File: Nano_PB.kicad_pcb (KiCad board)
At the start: 2 copper layers, 100 x 50 mm, 134 parts, among them CON1 BARREL_JACK, P1 CONN_02X04, P10 CONN_01X04, P11 CONN_01X04, P12 CONN_01X04, P2 CONN_01X06, P3 CONN_01X01, P4 CONN_01X03, P5 CONN_01X03, P6 CONN_01X03, P7 CONN_01X03, P8 CONN_01X03, P9 CONN_01X04, Q1 SMBT3904, Q2 SMBT3904, Q3 SMBT3904, Q4 SMBT3904, Q5 SMBT3904, Q6 BSS138, Q7 BSS138, SW1 Izquierda, SW2 Arriba, SW3 Abajo, SW4 Derecha, U1 Arduino_Nano, U2 LM7805CT, U3 74HC595, U4 74HC595, U5 Matriz_5x7, U6 PCA9551, U7 74HC148, U8 MMA7660FC, U9 40106

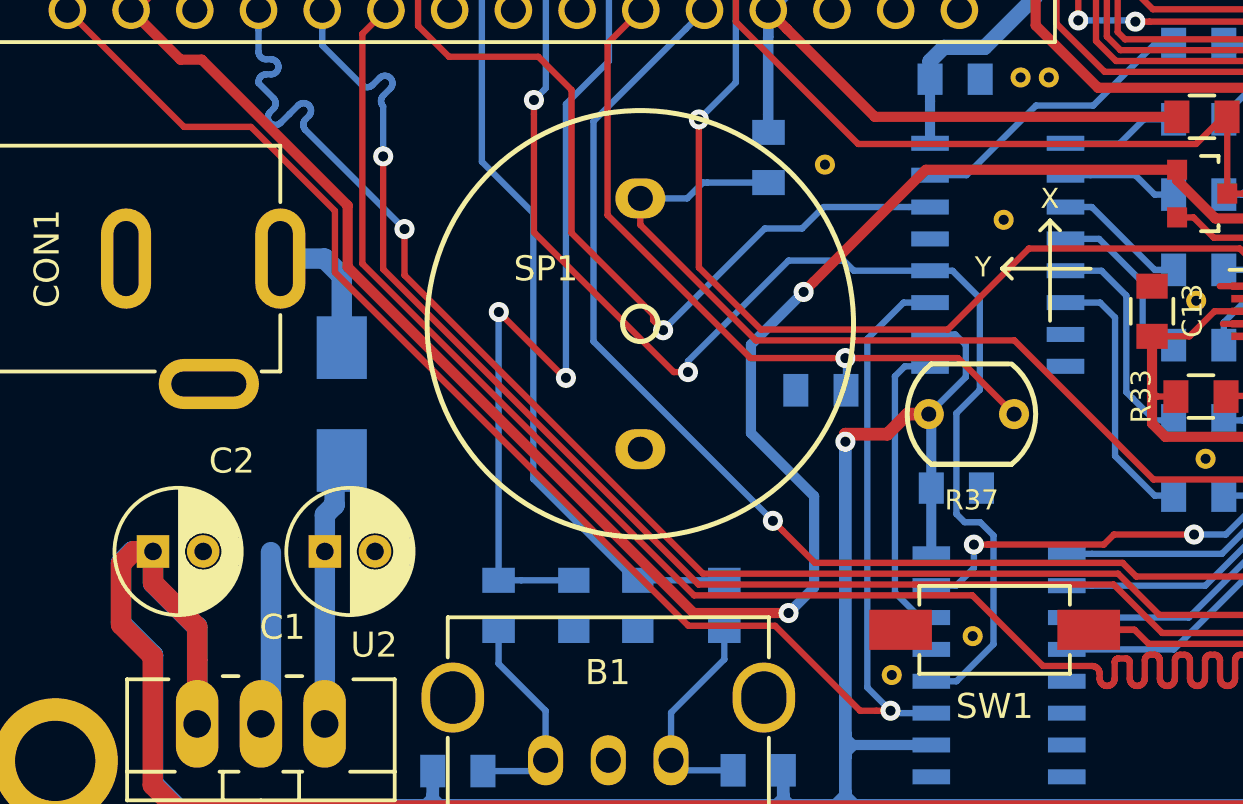
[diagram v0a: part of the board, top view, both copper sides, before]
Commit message: completar serigrafias
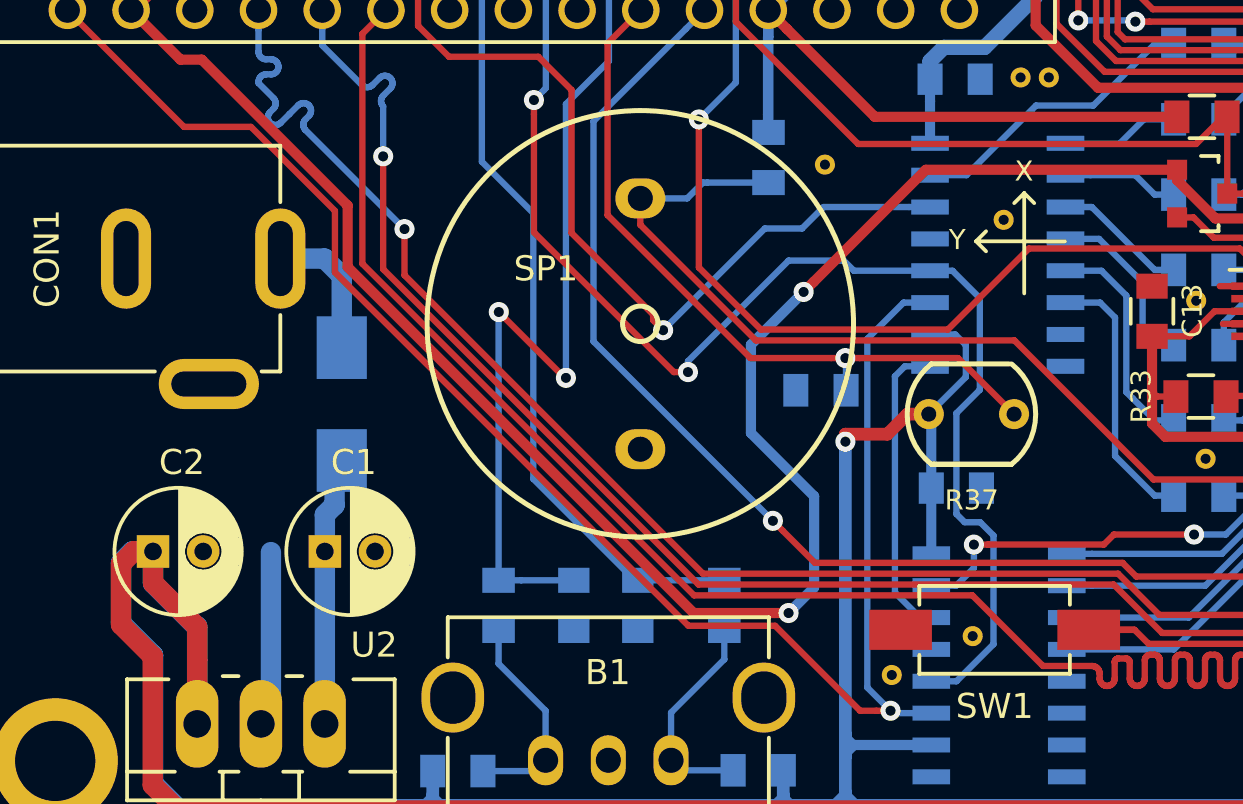
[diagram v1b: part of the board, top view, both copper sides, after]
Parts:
- moved G*** 1.10 mm to (62.9, 35.6)
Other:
- board text added: "3V3"
- board text added: "B0-A0"
- board text added: "B1-A1"
- board text added: "Bu-Ch5"
- board text added: "Buzz-Ch7"
- board text added: "Ch0"
- board text added: "Ch1"
- board text added: "Ch2"
- board text added: "Ch3"
- board text added: "ChB-D5"
- board text added: "Gn-Ch6"
- board text added: "Pul-A2"
- board text added: "Rd-Ch4"
- board text added: "TxD-D10 / RxD-D11"
- board text removed: "Bu-D11"
- board text removed: "Buzz-Ch8"
- board text removed: "Ch 1"
- board text removed: "Ch 2"
- board text removed: "Ch 3"
- board text removed: "Ch 4"
- board text removed: "ChB-A2"
- board text removed: "Gn-D10"
- board text removed: "Rd-D9"
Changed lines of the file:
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@@
     (links 268)
     (no_connects 0)
-    (area 49.508999 21.7677 161.770237 78.4273)
+    (area 52.014999 24.694999 152.165001 74.845001)
     (thickness 1.6)
-    (drawings 64)
+    (drawings 72)
     (tracks 1715)
     (zones 0)
@@
   )
   (module logos:KiCad-Logo_11mmx5mm (layer B.Cu)
-    (at 62.1 34.85 180)
+    (at 62.93 35.57 180)
     (fp_text reference G*** (at -0.8 1.6 180) (layer Cmts.User)
       (effects (font (size 0.3 0.3) (thickness 0.03)))
@@
     (descr "Radial Electrolytic Capacitor 5mm x Length 11mm, Pitch 2mm")
     (tags "Electrolytic Capacitor")
-    (fp_text reference C1 (at -1.69 3.02) (layer F.SilkS)
+    (fp_text reference C1 (at 1.15 -3.55) (layer F.SilkS)
       (effects (font (size 1 1) (thickness 0.15)))
     )
@@
     (descr "Radial Electrolytic Capacitor 5mm x Length 11mm, Pitch 2mm")
     (tags "Electrolytic Capacitor")
-    (fp_text reference C2 (at 3.14 -3.605) (layer F.SilkS)
+    (fp_text reference C2 (at 1.15 -3.55) (layer F.SilkS)
       (effects (font (size 1 1) (thickness 0.15)))
     )
@@
     )
   )
+  (gr_text Pul-A2 (at 130.856191 73.31) (layer B.SilkS)
+    (effects (font (size 1 1) (thickness 0.15)) (justify mirror))
+  )
+  (gr_text B1-A1 (at 131.094286 71.755) (layer B.SilkS)
+    (effects (font (size 1 1) (thickness 0.15)) (justify mirror))
+  )
+  (gr_text B0-A0 (at 131.094286 70.2) (layer B.SilkS)
+    (effects (font (size 1 1) (thickness 0.15)) (justify mirror))
+  )
+  (gr_text "TxD-D10 / RxD-D11" (at 104.85 26.58) (layer B.SilkS)
+    (effects (font (size 1 1) (thickness 0.15)) (justify mirror))
+  )
+  (gr_text Gnd (at 111.73 32.12) (layer B.SilkS)
+    (effects (font (size 1 1) (thickness 0.15)) (justify mirror))
+  )
+  (gr_text RxD (at 98.14 32) (layer B.SilkS)
+    (effects (font (size 1 1) (thickness 0.15)) (justify mirror))
+  )
+  (gr_text TxD (at 111.67 29.59) (layer B.SilkS)
+    (effects (font (size 1 1) (thickness 0.15)) (justify mirror))
+  )
+  (gr_text 3V3 (at 98.163809 29.43) (layer B.SilkS)
+    (effects (font (size 1 1) (thickness 0.15)) (justify mirror))
+  )
   (gr_text Izq-D6 (at 148.275 30.575) (layer B.SilkS)
     (effects (font (size 1 1) (thickness 0.15)) (justify mirror))
@@
     (effects (font (size 1 1) (thickness 0.15)) (justify mirror))
   )
-  (gr_text "Ch 1" (at 120.45 27.65) (layer B.SilkS)
+  (gr_text Ch0 (at 120.54 27.7) (layer B.SilkS)
     (effects (font (size 1 1) (thickness 0.15)) (justify mirror))
   )
-  (gr_text "Ch 2" (at 120.45 30.825) (layer B.SilkS)
+  (gr_text Ch1 (at 120.54 30.875) (layer B.SilkS)
     (effects (font (size 1 1) (thickness 0.15)) (justify mirror))
   )
@@
   (gr_line (start 52.09 24.77) (end 152.09 24.77) (layer Edge.Cuts) (width 0.15))
   (gr_line (start 52.09 34.77) (end 52.09 24.77) (layer Edge.Cuts) (width 0.15))
-  (gr_text Y (at 91.655 52.51) (layer F.SilkS)
+  (gr_text Y (at 90.625 51.42) (layer F.SilkS)
     (effects (font (size 0.8 0.8) (thickness 0.15)))
   )
-  (gr_text X (at 94.315 49.78) (layer F.SilkS)
+  (gr_text X (at 93.285 48.69) (layer F.SilkS)
     (effects (font (size 0.8 0.8) (thickness 0.15)))
   )
-  (gr_line (start 94.325 52.575) (end 95.945 52.575) (layer F.SilkS) (width 0.15))
-  (gr_line (start 92.405 52.57) (end 92.805 52.97) (layer F.SilkS) (width 0.15))
-  (gr_line (start 92.405 52.57) (end 92.805 52.17) (layer F.SilkS) (width 0.15))
-  (gr_line (start 94.325 52.57) (end 92.405 52.57) (layer F.SilkS) (width 0.15))
-  (gr_line (start 94.325 50.65) (end 94.725 51.05) (layer F.SilkS) (width 0.15))
-  (gr_line (start 93.925 51.05) (end 94.325 50.65) (layer F.SilkS) (width 0.15))
-  (gr_line (start 94.325 50.65) (end 94.325 54.65) (layer F.SilkS) (width 0.15))
-  (gr_text "Ch 3" (at 120.45 34) (layer B.SilkS)
+  (gr_line (start 93.295 51.485) (end 94.915 51.485) (layer F.SilkS) (width 0.15))
+  (gr_line (start 91.375 51.48) (end 91.775 51.88) (layer F.SilkS) (width 0.15))
+  (gr_line (start 91.375 51.48) (end 91.775 51.08) (layer F.SilkS) (width 0.15))
+  (gr_line (start 93.295 51.48) (end 91.375 51.48) (layer F.SilkS) (width 0.15))
+  (gr_line (start 93.295 49.56) (end 93.695 49.96) (layer F.SilkS) (width 0.15))
+  (gr_line (start 92.895 49.96) (end 93.295 49.56) (layer F.SilkS) (width 0.15))
+  (gr_line (start 93.295 49.56) (end 93.295 53.56) (layer F.SilkS) (width 0.15))
+  (gr_text Ch2 (at 120.54 34.05) (layer B.SilkS)
     (effects (font (size 1 1) (thickness 0.15)) (justify mirror))
   )
-  (gr_text "Ch 4" (at 120.45 37.175) (layer B.SilkS)
+  (gr_text Ch3 (at 120.54 37.225) (layer B.SilkS)
     (effects (font (size 1 1) (thickness 0.15)) (justify mirror))
   )
@@
     (effects (font (size 1 1) (thickness 0.15)) (justify mirror))
   )
-  (gr_text ChB-A2 (at 56.6 67.65) (layer B.SilkS)
+  (gr_text ChB-D5 (at 65.91 67.61) (layer B.SilkS)
     (effects (font (size 1 1) (thickness 0.15)) (justify mirror))
   )
-  (gr_text ChA-D2 (at 56.61 66.12) (layer B.SilkS)
+  (gr_text ChA-D2 (at 65.92 66.08) (layer B.SilkS)
     (effects (font (size 1 1) (thickness 0.15)) (justify mirror))
   )
@@
     (effects (font (size 1.2 1.2) (thickness 0.25) italic))
   )
-  (gr_text Buzz-Ch8 (at 75.5 57.5) (layer B.SilkS)
+  (gr_text Buzz-Ch7 (at 75.5 57.5) (layer B.SilkS)
     (effects (font (size 1 1) (thickness 0.15)) (justify mirror))
   )
-  (gr_text Bu-D11 (at 136.21 42.285) (layer B.SilkS)
+  (gr_text Bu-Ch5 (at 134.596191 41.345) (layer B.SilkS)
     (effects (font (size 1 1) (thickness 0.15)) (justify mirror))
   )
-  (gr_text Gn-D10 (at 136.21 40.63) (layer B.SilkS)
+  (gr_text Gn-Ch6 (at 134.596191 42.9) (layer B.SilkS)
     (effects (font (size 1 1) (thickness 0.15)) (justify mirror))
   )
-  (gr_text Rd-D9 (at 136.686191 38.975) (layer B.SilkS)
+  (gr_text Rd-Ch4 (at 134.596191 39.79) (layer B.SilkS)
     (effects (font (size 1 1) (thickness 0.15)) (justify mirror))
   )

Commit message: modificada posicion transistores bus I2C
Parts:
- moved Q7 0.68 mm to (99.7, 49.6)
- moved R35 0.68 mm to (99.7, 46.5)
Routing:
- net +5V: track 697.7 -> 690.3 mm, vias 2 -> 1
- net +3V3: track 181.8 -> 179.8 mm
- net A5: track 57.4 -> 56.7 mm
- net Net-(Q7-Pad2): track 13.9 -> 14.6 mm

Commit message: ultimas modificaciones a la PCB
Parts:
- removed the Gnd-Via at (149.6, 27.2)
- removed the Gnd-Via at (54.7, 72.2)
- removed the Gnd-Via at (149.5, 72.2)
- removed the Gnd-Via at (54.6, 31.6)
- added Gnd-Via: VAL**, Vias:Gnd-Via, F.Cu at (122.5, 58.5)
- added Gnd-Via: VAL**, Vias:Gnd-Via, F.Cu at (92.7, 54.0)
- added Gnd-Via: VAL**, Vias:Gnd-Via, F.Cu at (104.1, 64.6)
- added Gnd-Via: VAL**, Vias:Gnd-Via, F.Cu at (100.6, 70.7)
- added REF**: MountingHole_3.2mm_M3_DIN965, Mounting_Holes:MountingHole_3.2mm_M3_DIN965, F.Cu at (54.5, 32.7)
- added REF**: MountingHole_3.2mm_M3_DIN965, Mounting_Holes:MountingHole_3.2mm_M3_DIN965, F.Cu at (54.7, 72.2)
- added REF**: MountingHole_3.2mm_M3_DIN965, Mounting_Holes:MountingHole_3.2mm_M3_DIN965, F.Cu at (149.5, 72.2)
- added REF**: MountingHole_3.2mm_M3_DIN965, Mounting_Holes:MountingHole_3.2mm_M3_DIN965, F.Cu at (149.6, 27.2)
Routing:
- net GND: track 11.4 -> 4.67 mm
- net RESET: track 33.0 -> 34.2 mm
- net Net-(R30-Pad2): track 13.1 -> 13.9 mm
- net Net-(R1-Pad1): track 29.6 -> 30.3 mm
- net D6: track 77.0 -> 76.4 mm
- net Net-(R3-Pad1): track 34.4 -> 34.9 mm
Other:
- board text removed: "Pwm"

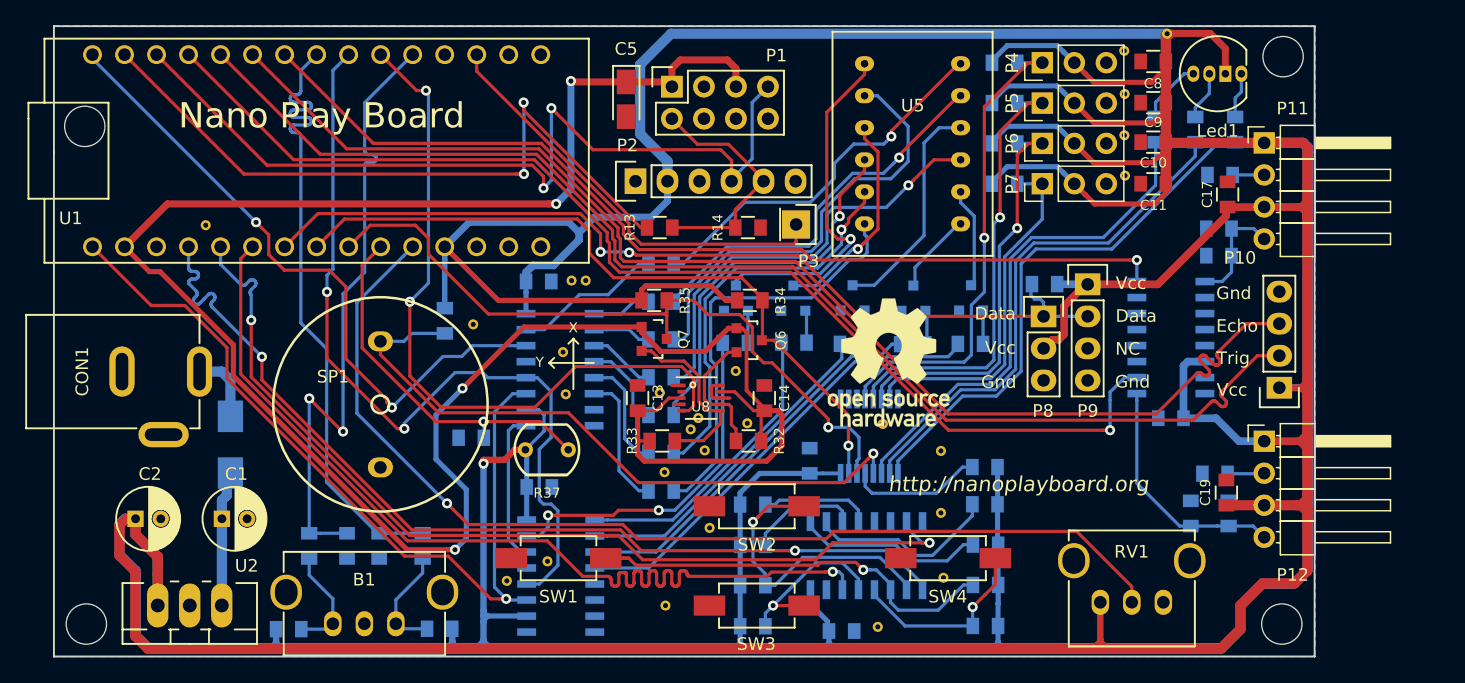
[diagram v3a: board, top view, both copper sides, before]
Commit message: finalizada la ubicacion de componentes para la V0.4
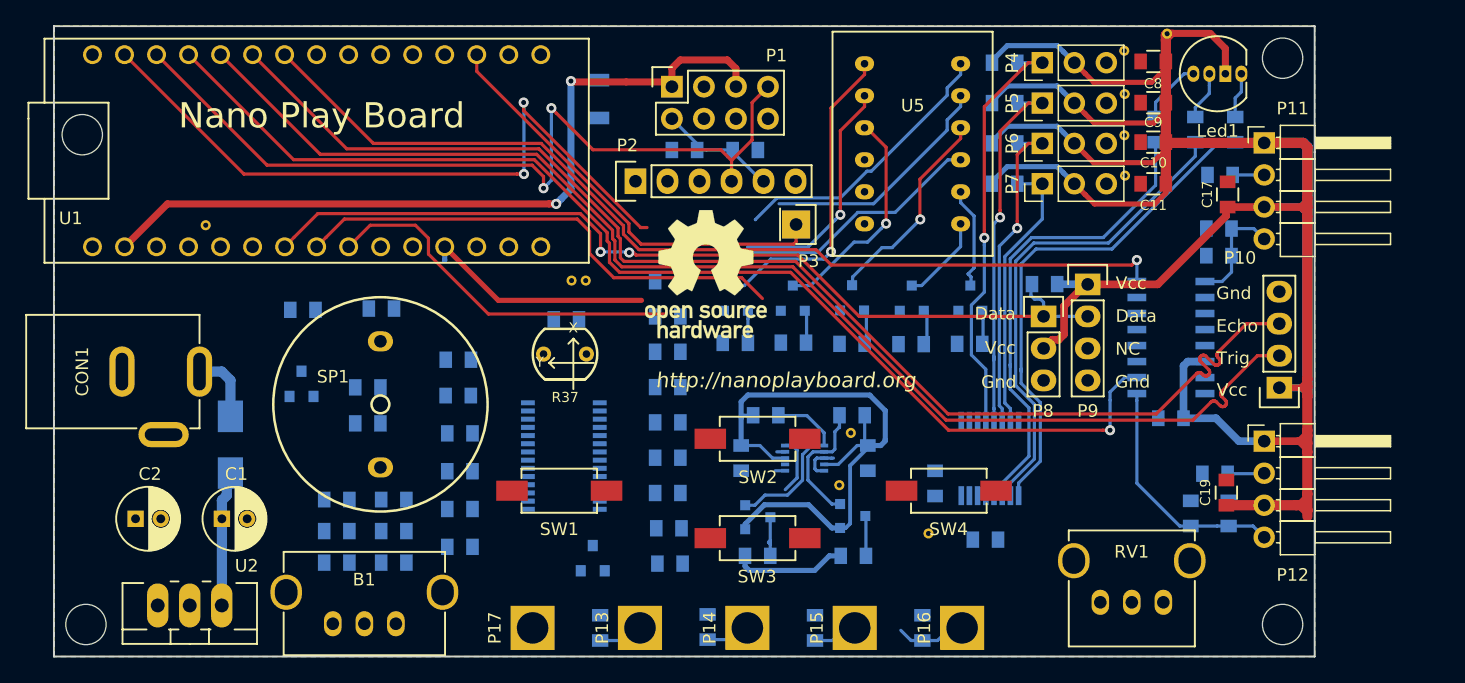
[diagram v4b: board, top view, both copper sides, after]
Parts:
- removed C12, C4: 100n, Capacitors_SMD:C_0805
- removed the Gnd-Via at (122.5, 58.5)
- removed the Gnd-Via at (85.3, 48.4)
- removed the Gnd-Via at (102.6, 56.8)
- removed the Gnd-Via at (92.5, 50.6)
- removed the Gnd-Via at (117.8, 56.3)
- removed the Gnd-Via at (117.4, 72.4)
- removed the Gnd-Via at (88.0, 68.8)
- removed the Gnd-Via at (92.7, 54.0)
- removed the Gnd-Via at (91.2, 67.2)
- removed the Gnd-Via at (103.2, 55.9)
- removed the Gnd-Via at (104.1, 64.6)
- removed the Gnd-Via at (100.6, 70.7)
- removed the Gnd-Via at (103.7, 58.4)
- removed the Gnd-Via at (100.5, 60.1)
- removed the Gnd-Via at (100.2, 53.9)
- removed the Gnd-Via at (122.7, 68.5)
- removed U4: 74HC595, Housings_SOIC:SOIC-16_3.9x9.9mm_Pitch1.27mm
- removed U7: 74HC148, Housings_SOIC:SOIC-16_3.9x9.9mm_Pitch1.27mm
- added P13: CONN_01X01, Conectores:Pad_Conector_Cocodrilo, F.Cu at (98.6, 72.5)
- added P14: CONN_01X01, Conectores:Pad_Conector_Cocodrilo, F.Cu at (107.1, 72.5)
- added P15: CONN_01X01, Conectores:Pad_Conector_Cocodrilo, F.Cu at (115.6, 72.5)
- added P16: CONN_01X01, Conectores:Pad_Conector_Cocodrilo, F.Cu at (124.1, 72.5)
- added P17: CONN_01X01, Conectores:Pad_Conector_Cocodrilo, F.Cu at (90.1, 72.5)
- added Q8: SMBT3904, TO_SOT_Packages_SMD:SOT-23, B.Cu at (71.7, 53.1)
- added Q9: SMBT3904, TO_SOT_Packages_SMD:SOT-23, B.Cu at (94.8, 67.0)
- added R47: 10K, Resistencias:R_0805, B.Cu at (84.2, 51.2)
- added R48: 47K, Resistencias:R_0805, B.Cu at (77.0, 56.3)
- added R49: 1K, Resistencias:R_0805, B.Cu at (77.0, 53.4)
- added R50: 10K, Resistencias:R_0805, B.Cu at (71.8, 47.3)
- added R51: 47K, Resistencias:R_0805, B.Cu at (101.0, 67.4)
- added R52: 1K, Resistencias:R_0805, B.Cu at (100.9, 64.6)
- C13, C14, Gnd-Via (x2), Q6, Q7, R13, R14, R32, R33, R34, R35, U8: moved to B.Cu
- C5: value 10u -> 47u; footprint Capacitors_Tantalum_SMD:Tantalum_Case-A_EIA-3216-18_Reflow -> Capacitors_SMD:C_1206; moved to B.Cu
- R28, R29, R30, R31: value 10K -> 10M
- U3: value 74HC595 -> MCP23017; footprint Housings_SOIC:SOIC-16_3.9x9.9mm_Pitch1.27mm -> Housings_SSOP:TSSOP-28_4.4x9.7mm_Pitch0.65mm
- moved R26 42.7 mm to (84.3, 60.1), turned to 0 degrees
- moved R27 42.0 mm to (84.3, 57.1)
- moved R25 41.8 mm to (84.3, 63.1)
- moved R28 30.6 mm to (95.4, 72.5), turned to 270 degrees
- moved R24 23.4 mm to (84.3, 66.1)
- moved R34 21.9 mm to (115.5, 66.8)
- moved R35 21.9 mm to (107.9, 66.8)
- moved R31 16.6 mm to (121.0, 72.5), turned to 270 degrees
- moved Q7 16.4 mm to (107.9, 63.7), turned to 90 degrees
- moved Q6 16.2 mm to (115.5, 63.6), turned to 90 degrees
- moved G*** 16.1 mm to (103.8, 44.4)
- moved Gnd-Via 12.2 mm to (114.4, 61.2)
- moved R38 12.1 mm to (92.7, 48.0)
- moved C7 10.1 mm to (122.0, 61.0)
- moved U6 9.73 mm to (126.3, 59.1)
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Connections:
- P8 pad 1: A3 -> D12
- P9 pad 2: A3 -> D12
- R1 pad 2: Net-(R1-Pad2) -> PA0
- R10 pad 2: Net-(R10-Pad2) -> PB1
- R11 pad 2: Net-(R11-Pad2) -> PB2
- R12 pad 2: Net-(R12-Pad2) -> PB3
- R15 pad 2: Net-(R15-Pad2) -> ~RESET
- R2 pad 2: Net-(R2-Pad2) -> PA1
- R23 pad 2: A3 -> D12
- R24 pad 2: Net-(R24-Pad2) -> PB4
- R25 pad 1: Net-(R25-Pad1) -> +5V
- R25 pad 2: +5V -> PB5
- R26 pad 2: Net-(R26-Pad2) -> PB6
- R27 pad 1: Net-(R27-Pad1) -> +5V
- R27 pad 2: +5V -> PB7
- R28 pad 2: Net-(R28-Pad2) -> A0
- R29 pad 1: Net-(R29-Pad1) -> +5V
- R29 pad 2: +5V -> A1
- R3 pad 2: Net-(R3-Pad2) -> PA2
- R30 pad 2: Net-(R30-Pad2) -> A2
- R31 pad 1: Net-(R31-Pad1) -> +5V
- R31 pad 2: +5V -> A3
- R4 pad 2: Net-(R4-Pad2) -> PA3
- R5 pad 2: Net-(R5-Pad2) -> PA4
- R6 pad 2: Net-(R6-Pad2) -> PA5
- R7 pad 2: Net-(R7-Pad2) -> PA6
- R8 pad 2: Net-(R8-Pad2) -> PA7
- R9 pad 2: Net-(R9-Pad2) -> PB0
- SW1 pad 2: Net-(R26-Pad2) -> PB5
- SW2 pad 2: Net-(R24-Pad2) -> PB4
- SW3 pad 2: Net-(R30-Pad2) -> PB7
- SW4 pad 2: Net-(R28-Pad2) -> PB6
- U1 pad 16: D13 -> Net-(U1-Pad16)
- U1 pad 7: D4 -> ~RESET
- U3 pad 1: Net-(R2-Pad2) -> PB0
- U3 pad 10: +5V -> GND
- U3 pad 11: D13 -> (no net)
- U3 pad 12: D4 -> A5
- U3 pad 13: GND -> A4
- U3 pad 14: D12 -> (no net)
- U3 pad 15: Net-(R1-Pad2) -> GND
- U3 pad 2: Net-(R3-Pad2) -> PB1
- U3 pad 3: Net-(R4-Pad2) -> PB2
- U3 pad 4: Net-(R5-Pad2) -> PB3
- U3 pad 5: Net-(R6-Pad2) -> PB4
- U3 pad 6: Net-(R7-Pad2) -> PB5
- U3 pad 7: Net-(U3-Pad7) -> PB6
- U3 pad 8: GND -> PB7
- U3 pad 9: Net-(U3-Pad9) -> +5V
- U6 pad 13: Net-(R15-Pad2) -> ~RESET
- U8 pad 5: D3 -> Net-(R52-Pad1)
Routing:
- net +5V: track 690.3 -> 252.0 mm, vias 1 -> 0
- net A7: track 83.9 -> 0.00 mm, vias 1 -> 0
- net A2: track 76.0 -> 3.57 mm, vias 1 -> 0
- net A0: track 76.0 -> 3.57 mm, vias 2 -> 0
- net A1: track 76.0 -> 4.17 mm, vias 2 -> 0
- net +3V3: track 179.7 -> 110.9 mm, vias 4 -> 2
- net D4: track 66.0 -> 0.00 mm, vias 2 -> 0
- net D13: track 65.8 -> 0.00 mm, vias 1 -> 0
- net D3: track 56.7 -> 0.00 mm, vias 2 -> 0
- net BUZZER: track 52.3 -> 0.00 mm, vias 1 -> 0
- net D5: track 51.5 -> 0.00 mm
- net D2: track 51.0 -> 0.00 mm, vias 2 -> 0
- net A3: track 72.2 -> 30.2 mm, vias 2 -> 0
- net Net-(R12-Pad2): track 36.4 -> 0.00 mm
- net Net-(R26-Pad2): track 35.4 -> 0.00 mm, vias 1 -> 0
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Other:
- board text added: "Rev-0.4.0"
- board text removed: "B0-A0"
- board text removed: "B1-A1"
- board text removed: "ClkIn-D13"
- board text removed: "ClkOut-D4"
- board text removed: "Din-D12"
- board text removed: "Pul-A2"
- board text removed: "Rev-0.3.0"
